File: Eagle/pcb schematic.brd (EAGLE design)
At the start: 100 x 80 mm, 21 parts

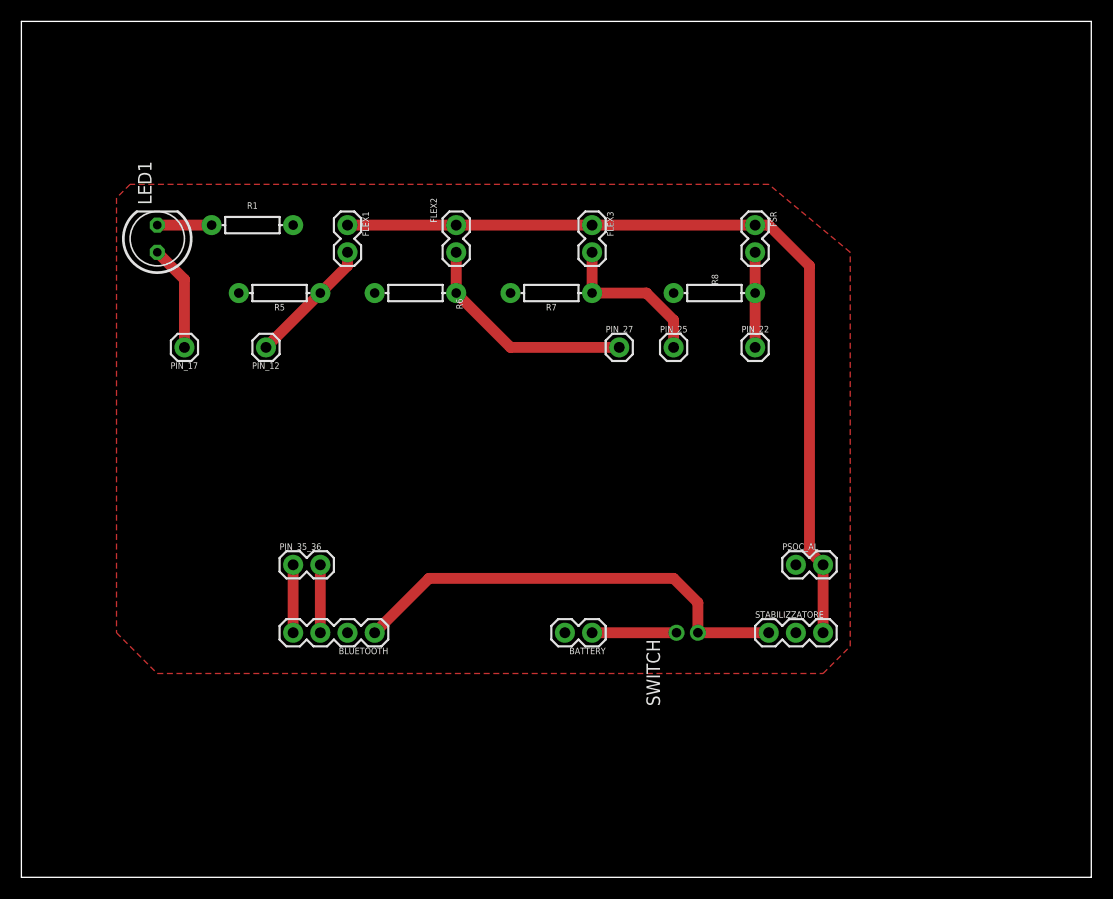
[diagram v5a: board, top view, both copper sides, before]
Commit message: PCB con aggiunta resistenze per carica batteria
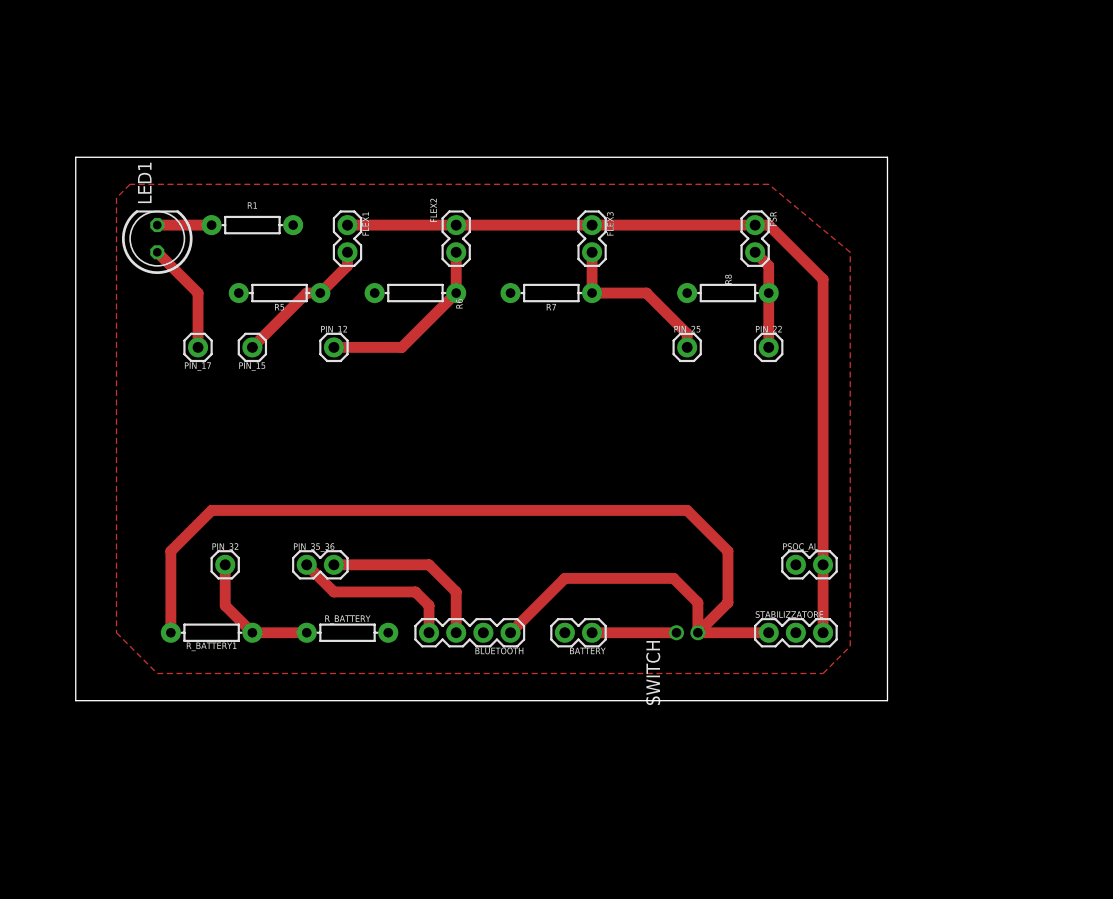
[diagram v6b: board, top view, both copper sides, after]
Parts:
- removed PIN_27: (no value), SparkFun-Connectors:1X01
- added PIN_15, PIN_32: (no value), SparkFun-Connectors:1X01
- added R_BATTERY, R_BATTERY1: (no value), SparkFun-Resistors:AXIAL-0.3
- moved BLUETOOTH 12.7 mm to (45.7, 22.9)
- moved PIN_12 6.35 mm to (29.2, 49.5), turned to 0 degrees
- moved R8 1.27 mm to (66.0, 54.6)
- moved PIN_35_36 1.27 mm to (26.7, 29.2)
- moved PIN_17 1.27 mm to (16.5, 49.5)
- moved PIN_22 1.27 mm to (69.8, 49.5)
- moved PIN_25 1.27 mm to (62.2, 49.5)
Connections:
- new net N$9: PIN_32.1, R_BATTERY.P$1, R_BATTERY1.P$2
- net GND: now also R_BATTERY.P$2
- net N$1: now also PIN_15.1; no longer PIN_12.1
- net N$10: now also R_BATTERY1.P$1
- net N$2: now also PIN_12.1; no longer PIN_27.1
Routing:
- net N$10: track 42.7 -> 101.6 mm
- net N$9: track 0.00 -> 12.5 mm
- net N$4: track 6.35 -> 16.3 mm
- net N$6: track 6.35 -> 15.5 mm
- net N$2: track 21.2 -> 17.3 mm
- net N$1: track 12.0 -> 13.3 mm
- net N$7: track 9.94 -> 10.5 mm
- net N$5: track 8.89 -> 9.42 mm
- net N$3: track 15.0 -> 15.5 mm
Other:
- board size 100 x 80 mm -> 75.9 x 50.8 mm
